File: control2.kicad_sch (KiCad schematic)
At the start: 16 parts, among them J8 AudioJack3_SwitchTR, J9 AudioJack3_SwitchTR, U10 USBLC6-2SC6, U4 74HC595, U6 74HC595, U7 74HC595, U8 74HC595, U9 USBLC6-2SC6

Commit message: Перевёл на иерархические схемы
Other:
- moved on the sheet: C30, C31, C32, C33, J8, J9, R10, R11, R12, R13, U10, U4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

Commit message: save state (add 1g logic)
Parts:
- added U12: SN74LVC1G125DBV, Package_TO_SOT_SMD:SOT-23-5, symbol 74xGxx:SN74LVC1G125DBV
- added U13: 74LVC1G32, Package_TO_SOT_SMD:SOT-23-5, symbol 74xGxx:74LVC1G32
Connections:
- net RFGND: now also U12.1, U12.3 (GND), U13.3 (GND)
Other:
- moved on the sheet: J8, J9

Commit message: save state
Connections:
- net DVDD_3P3: now reaches U12.5 (VCC)
- net DVDD_3P3: now also U13.5 (VCC)
- net DVDD_5P0: now reaches U9.5 (VBUS)
- net DVDD_5P0: now also U10.5 (VBUS)
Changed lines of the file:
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@@
+	(wire
+		(pts
+			(xy 138.43 86.36) (xy 138.43 93.98)
+		)
+		(stroke
+			(width 0)
+			(type default)
+		)
+	)
 	(wire
 		(pts
@@
 	(wire
 		(pts
+			(xy 120.65 140.97) (xy 120.65 146.05)
+		)
+		(stroke
+			(width 0)
+			(type default)
+		)
+	)
+	(wire
+		(pts
 			(xy 290.83 48.26) (xy 283.21 48.26)
 		)
@@
 	(wire
 		(pts
+			(xy 196.85 44.45) (xy 196.85 54.61)
+		)
+		(stroke
+			(width 0)
+			(type default)
+		)
+	)
+	(wire
+		(pts
+			(xy 138.43 52.07) (xy 138.43 59.69)
+		)
+		(stroke
+			(width 0)
+			(type default)
+		)
+	)
+	(wire
+		(pts
 			(xy 62.23 67.31) (xy 67.31 67.31)
 		)
@@
 		)
 	)
+	(label "DVDD_5P0"
+		(at 138.43 86.36 0)
+		(effects
+			(font
+				(size 1.27 1.27)
+			)
+			(justify left bottom)
+		)
+	)
 	(label "RFGND"
 		(at 161.29 72.39 0)
@@
 		)
 	)
+	(label "DVDD_3P3"
+		(at 196.85 44.45 0)
+		(effects
+			(font
+				(size 1.27 1.27)
+			)
+			(justify left bottom)
+		)
+	)
 	(label "RFGND"
 		(at 161.29 106.68 0)
 		(effects
 			(font
+				(size 1.27 1.27)
+			)
+			(justify left bottom)
+		)
+	)
+	(label "DVDD_3P3"
+		(at 120.65 140.97 0)
+		(effects
+			(font
+				(size 1.27 1.27)
+			)
+			(justify left bottom)
+		)
+	)
+	(label "DVDD_5P0"
+		(at 138.43 52.07 0)
+		(effects
+			(font

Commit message: save state
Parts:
- added U14: 74LVC1G32, Package_TO_SOT_SMD:SOT-23-5, symbol 74xGxx:74LVC1G32
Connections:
- net DVDD_3P3: now also U4.10 (~{SRCLR}), U4.16 (VCC), U6.10 (~{SRCLR}), U6.13 (~{OE}), U6.16 (VCC), U7.10 (~{SRCLR}), U7.16 (VCC), U8.10 (~{SRCLR}), U8.16 (VCC), U14.5 (VCC)
- net RFGND: now also U14.3 (GND)
- net at U4.11 (SRCLK), U6.11 (SRCLK), U7.11 (SRCLK)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: now also U14.4
- net at U4.12 (RCLK), U6.12 (RCLK), U7.12 (RCLK)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: now also U13.2, U14.2
- net at U6.9 (QH'): now also U7.14 (SER)
- net at U4.14 (SER): now also U13.4
- net at U7.9 (QH'): now also U8.14 (SER)
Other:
- moved on the sheet: U13

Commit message: Add ULN2003
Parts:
- added U15, U16, U17, U18: ULN2002A, Package_SO:TSSOP-16_4.4x5mm_P0.65mm, symbol Transistor_Array:ULN2002A
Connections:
- net RFGND: now also U15.8 (GND), U16.8 (GND), U17.8 (GND), U18.8 (GND)
- net at U6.1 (QB): now also U17.7 (I7)
- net at U6.2 (QC): now also U17.6 (I6)
- net at U6.3 (QD): now also U17.5 (I5)
- net at U6.4 (QE): now also U17.4 (I4)
- net at U6.5 (QF): now also U17.3 (I3)
- net at U6.6 (QG): now also U17.2 (I2)
- net at U6.7 (QH): now also U17.1 (I1)
- net at U4.1 (QB): now also U18.7 (I7)
- net at U4.2 (QC): now also U18.6 (I6)
- net at U4.3 (QD): now also U18.5 (I5)
- net at U4.4 (QE): now also U18.4 (I4)
- net at U4.5 (QF): now also U18.3 (I3)
- net at U4.6 (QG): now also U18.2 (I2)
- net at U4.7 (QH): now also U18.1 (I1)
- net at U7.1 (QB): now also U16.7 (I7)
- net at U7.2 (QC): now also U16.6 (I6)
- net at U7.3 (QD): now also U16.5 (I5)
- net at U7.4 (QE): now also U16.4 (I4)
- net at U7.5 (QF): now also U16.3 (I3)
- net at U7.6 (QG): now also U16.2 (I2)
- net at U7.7 (QH): now also U16.1 (I1)
- net at U8.1 (QB): now also U15.7 (I7)
- net at U8.2 (QC): now also U15.6 (I6)
- net at U8.3 (QD): now also U15.5 (I5)
- net at U8.4 (QE): now also U15.4 (I4)
- net at U8.5 (QF): now also U15.3 (I3)
- net at U8.6 (QG): now also U15.2 (I2)
- net at U8.7 (QH): now also U15.1 (I1)

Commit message: Использование power symbols
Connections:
- net DVDD_3P3 renamed DVDD1_3P3
- net DVDD_5P0 renamed DVDD1_5P0
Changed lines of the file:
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@@
+	(wire
+		(pts
+			(xy 68.58 161.29) (xy 78.74 161.29)
+		)
+		(stroke
+			(width 0)
+			(type default)
+		)
+	)
 	(wire
 		(pts
@@
 		(pts
 			(xy 335.28 48.26) (xy 311.15 48.26)
+		)
+		(stroke
+			(width 0)
+			(type default)
+		)
+	)
+	(wire
+		(pts
+			(xy 68.58 168.91) (xy 78.74 168.91)
 		)
 		(stroke
@@
 		)
 	)
+	(label "DVDD_3P3"
+		(at 78.74 168.91 0)
+		(effects
+			(font
+				(size 1.27 1.27)
+			)
+			(justify left bottom)
+		)
+	)
 	(label "RFGND"
 		(at 255.27 101.6 180)
@@
 	(label "DVDD_3P3"
 		(at 255.27 27.94 0)
+		(effects
+			(font
+				(size 1.27 1.27)
+			)
+			(justify left bottom)
+		)
+	)
+	(label "DVDD_5P0"
+		(at 78.74 161.29 0)
 		(effects
 			(font
@@
 			(hide yes)
 			(show_name no)
+			(do_not_autoplace no)
+			(effects
+				(font
+					(size 1.27 1.27)
+				)
+				(justify right)
+			)
+		)
+	)
+	(global_label "DVDD1_5P0"
+		(shape input)
+		(at 68.58 161.29 180)
+		(fields_autoplaced yes)
+		(effects
+			(font
+				(size 1.27 1.27)
+			)
+			(justify right)
+		)
+		(property "Intersheetrefs" "${INTERSHEET_REFS}"
+			(at 54.8301 161.29 0)
+			(hide yes)
+			(show_name no)
+			(do_not_autoplace no)
+			(effects
+				(font
+					(size 1.27 1.27)
+				)
+				(justify right)
+			)
+		)
+	)
+	(global_label "DVDD1_3P3"
+		(shape input)
+		(at 68.58 168.91 180)
+		(fields_autoplaced yes)
+		(effects
+			(font
+				(size 1.27 1.27)
+			)
+			(justify right)
+		)
+		(property "Intersheetrefs" "${INTERSHEET_REFS}"
+			(at 54.8301 168.91 0)
+			(hide yes)
+			(show_name no)

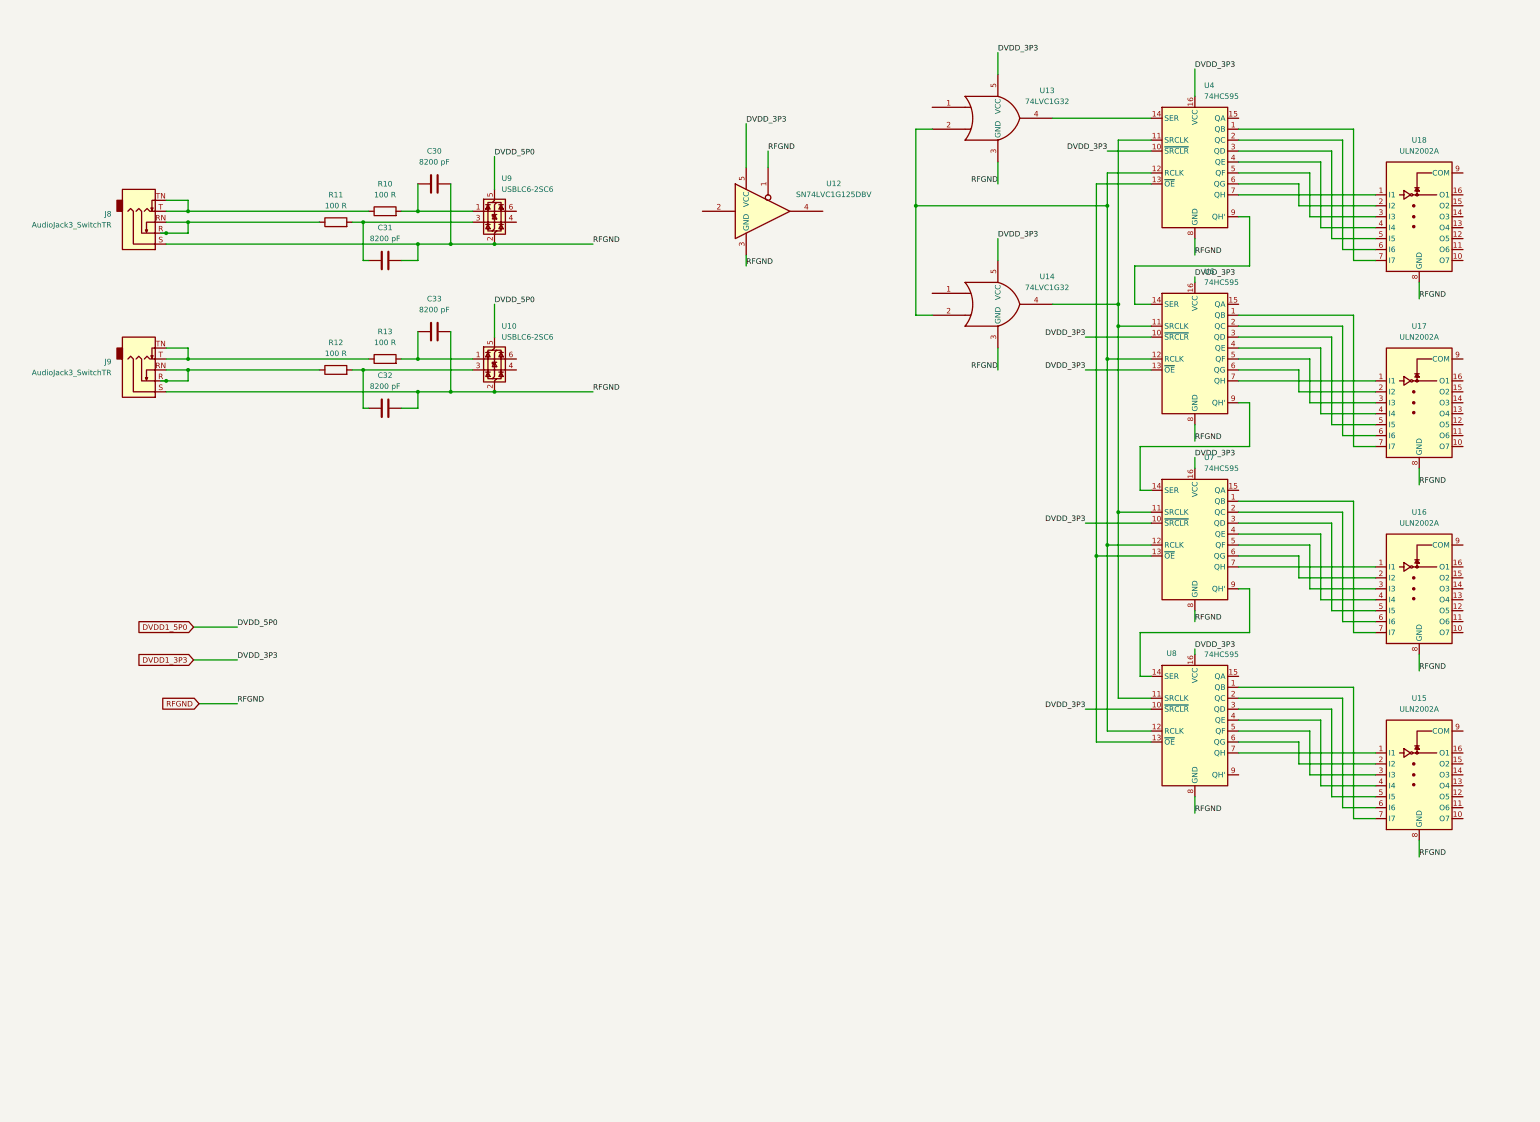
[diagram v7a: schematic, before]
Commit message: add lcd backlight chip
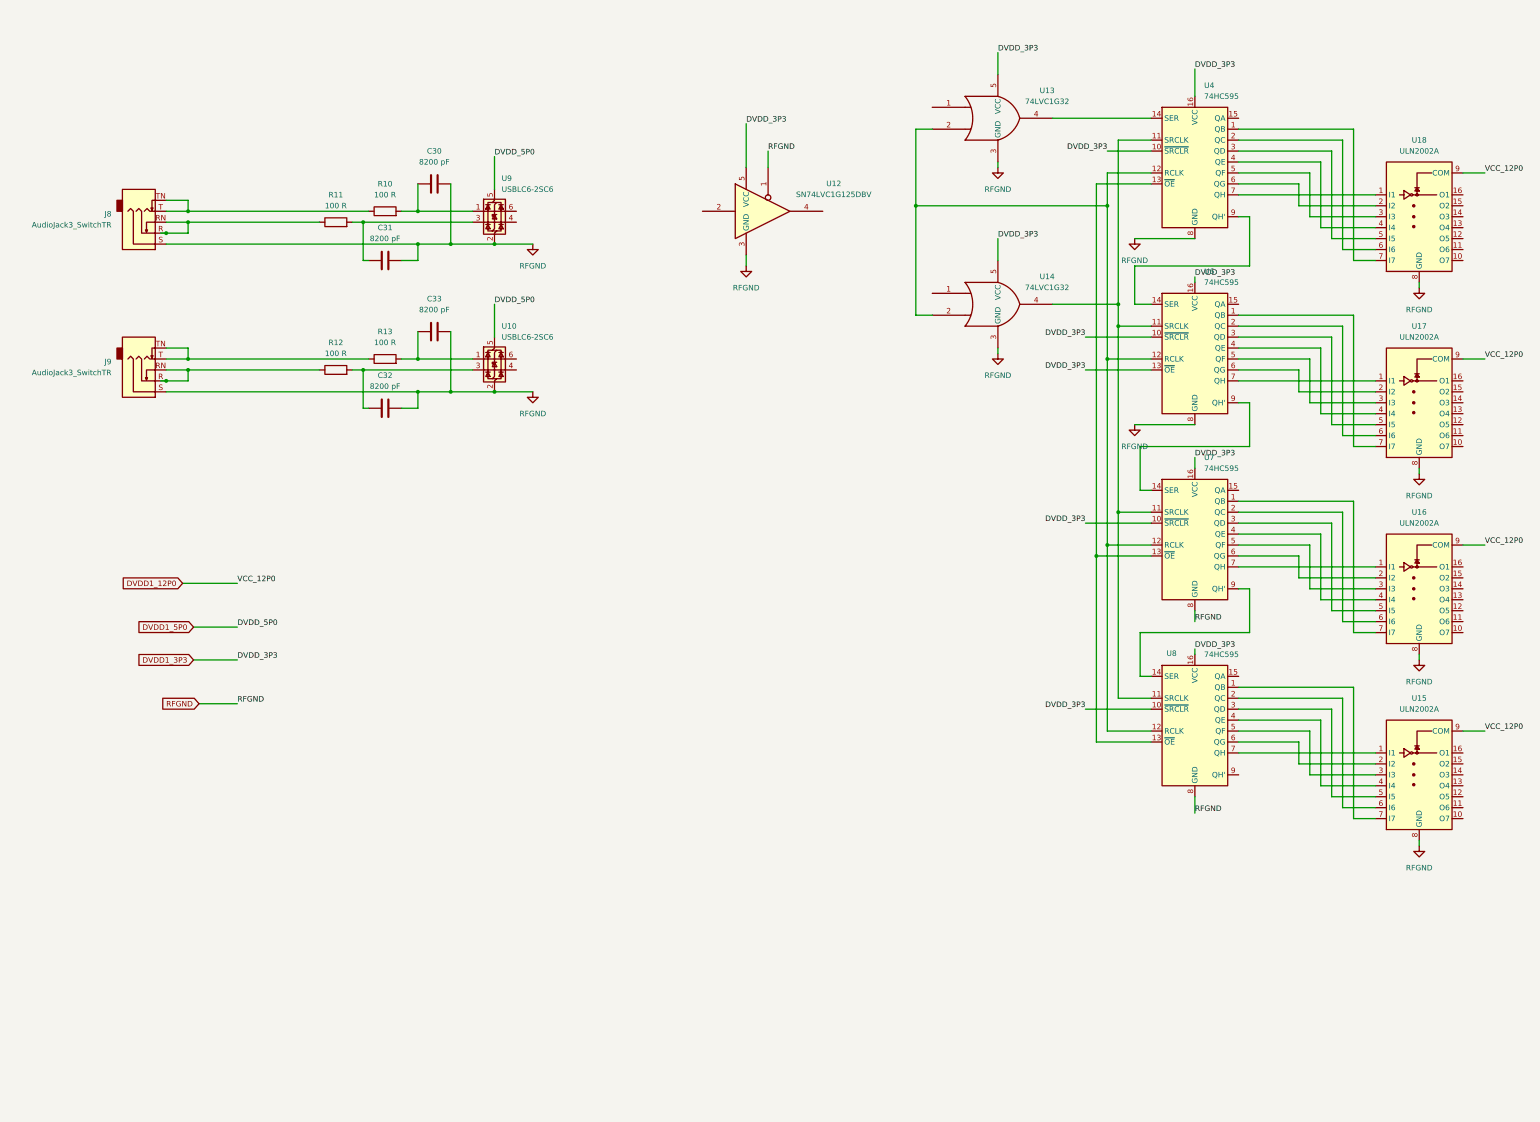
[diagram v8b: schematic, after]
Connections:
- net DVDD1_12P0: now reaches U15.9 (COM)
- net DVDD1_12P0: now also U16.9 (COM), U17.9 (COM), U18.9 (COM)
